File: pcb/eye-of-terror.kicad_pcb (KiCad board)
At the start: 4 copper layers, 200 x 200 mm, 225 parts, among them J1 Conn_01x02_Socket, J2 G-Switch GT-USB-7055E, J3 Conn_01x04, J4 Conn_01x04, J5 Conn_01x03, J6 Conn_01x02_Socket, J7 Conn_01x02_Socket, J8 Conn_01x03, Q1 IPT020N10N3, Q10 ALS-PT19-315C/L177/TR8, Q11 ALS-PT19-315C/L177/TR8, Q12 ALS-PT19-315C/L177/TR8, Q13 ALS-PT19-315C/L177/TR8, Q14 ALS-PT19-315C/L177/TR8, Q15 ALS-PT19-315C/L177/TR8, Q16 ALS-PT19-315C/L177/TR8, Q17 ALS-PT19-315C/L177/TR8, Q2 IPT020N10N3, Q3 IPT020N10N3, Q4 IPT020N10N3, Q5 IPT020N10N3, Q6 IPT020N10N3, Q7 ALS-PT19-315C/L177/TR8, Q8 ALS-PT19-315C/L177/TR8, Q9 ALS-PT19-315C/L177/TR8, SW1 SW_Push, SW2 SW_Push, U1 RP2350B, U2 TD1660, U3 AP63205WU-7, U4 LSM6DS3, U5 W25Q32JVSS, U7 DRV8353HRTAR, Y1 ABM8-272-T3

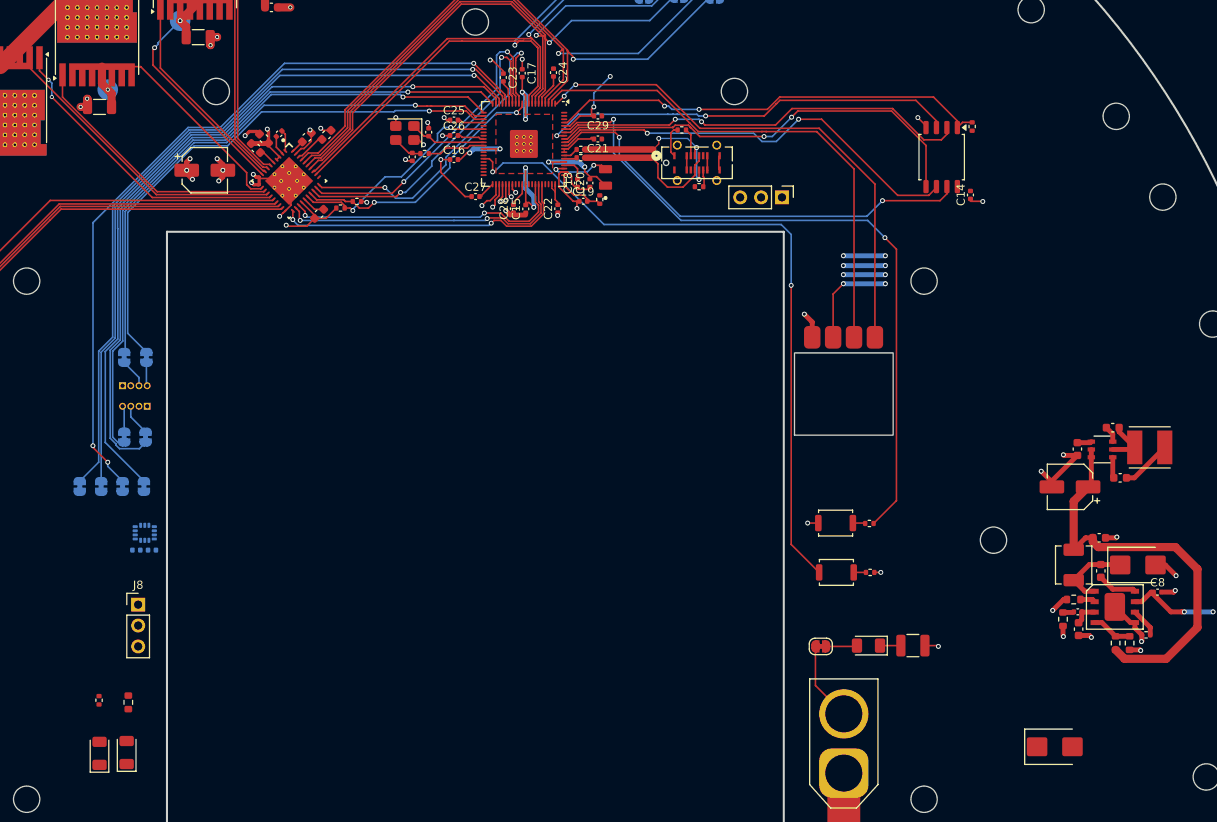
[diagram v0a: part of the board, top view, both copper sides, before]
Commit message: routed GPIO and debug LEDs
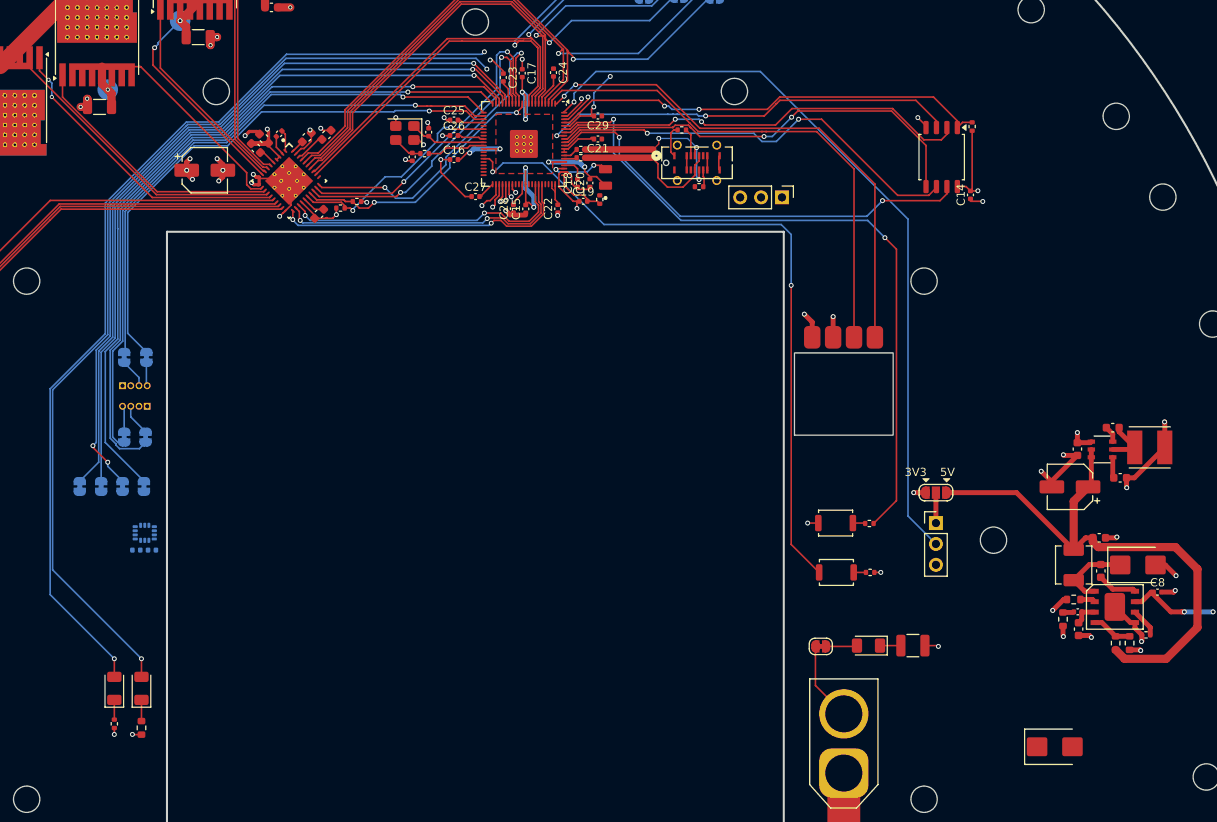
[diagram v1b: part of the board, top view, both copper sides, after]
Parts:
- added JP8: SolderJumper_3_Open, Jumper:SolderJumper-3_P1.3mm_Open_RoundedPad1.0x1.5mm_NumberLabels, F.Cu at (364.7, 193.3)
- moved J8 97.5 mm to (364.7, 197.0)
- moved D13 8.10 mm to (264.8, 217.1)
- moved D16 8.00 mm to (268.1, 217.1)
- moved R38 3.49 mm to (268.1, 221.9), turned to -90 degrees
- moved R35 3.41 mm to (264.8, 221.4), turned to -90 degrees
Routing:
- net /GREEN_LED_1: track 0.00 -> 138.1 mm, vias 0 -> 3
- net /BLUE_LED_1: track 0.00 -> 134.9 mm, vias 0 -> 3
- net /GPIO3: track 0.00 -> 92.9 mm, vias 0 -> 1
- net +5V: track 49.7 -> 68.0 mm
- net +3V3: track 82.8 -> 71.7 mm, vias 12 -> 10
- net Net-(J8-Pin_1): track 0.00 -> 3.70 mm
- net Net-(D16-K): track 0.00 -> 2.57 mm
- net Net-(D13-K): track 0.00 -> 2.40 mm
- net DGND: track 50.4 -> 52.2 mm, vias 20 -> 22
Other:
- board text added: "3V3"
- board text added: "5V"

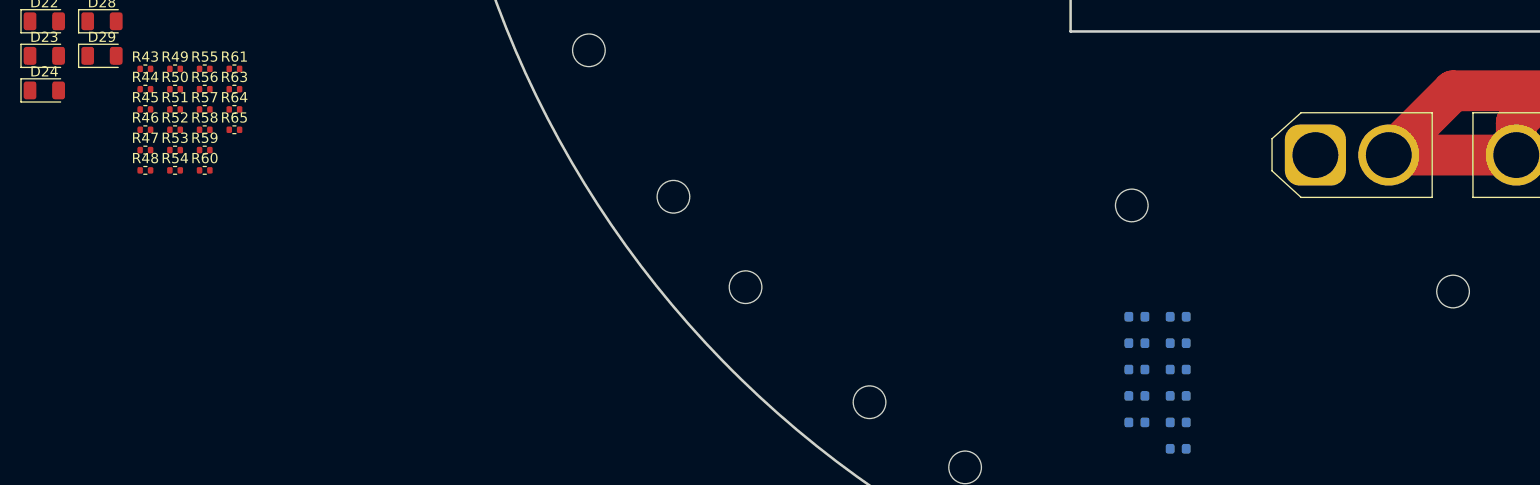
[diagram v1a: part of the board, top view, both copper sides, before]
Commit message: added placement dxf for encoders to layout
i think it lines up alright like this
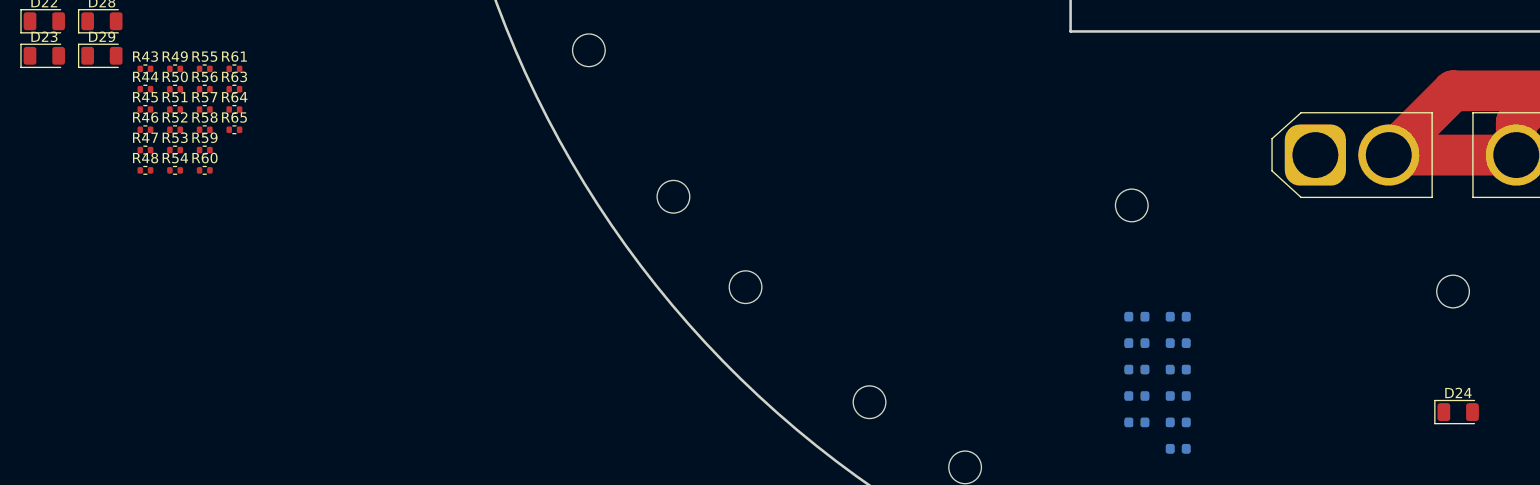
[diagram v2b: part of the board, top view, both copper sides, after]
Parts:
- moved D24 142.2 mm to (309.2, 273.9)

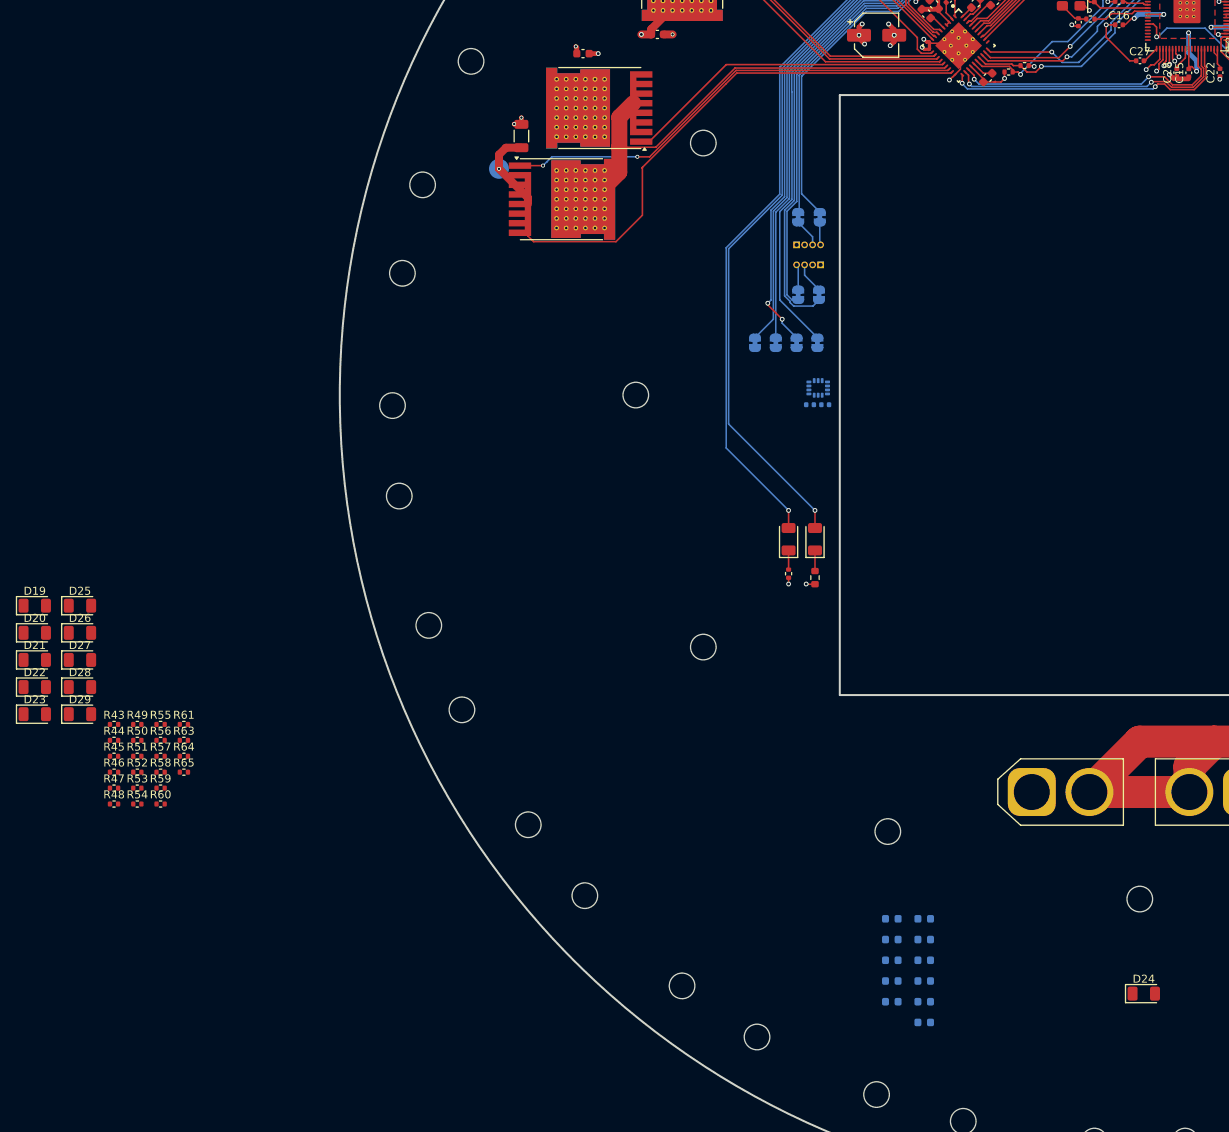
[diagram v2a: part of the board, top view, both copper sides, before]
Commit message: deleted 11th encoder pin (we only use 10)
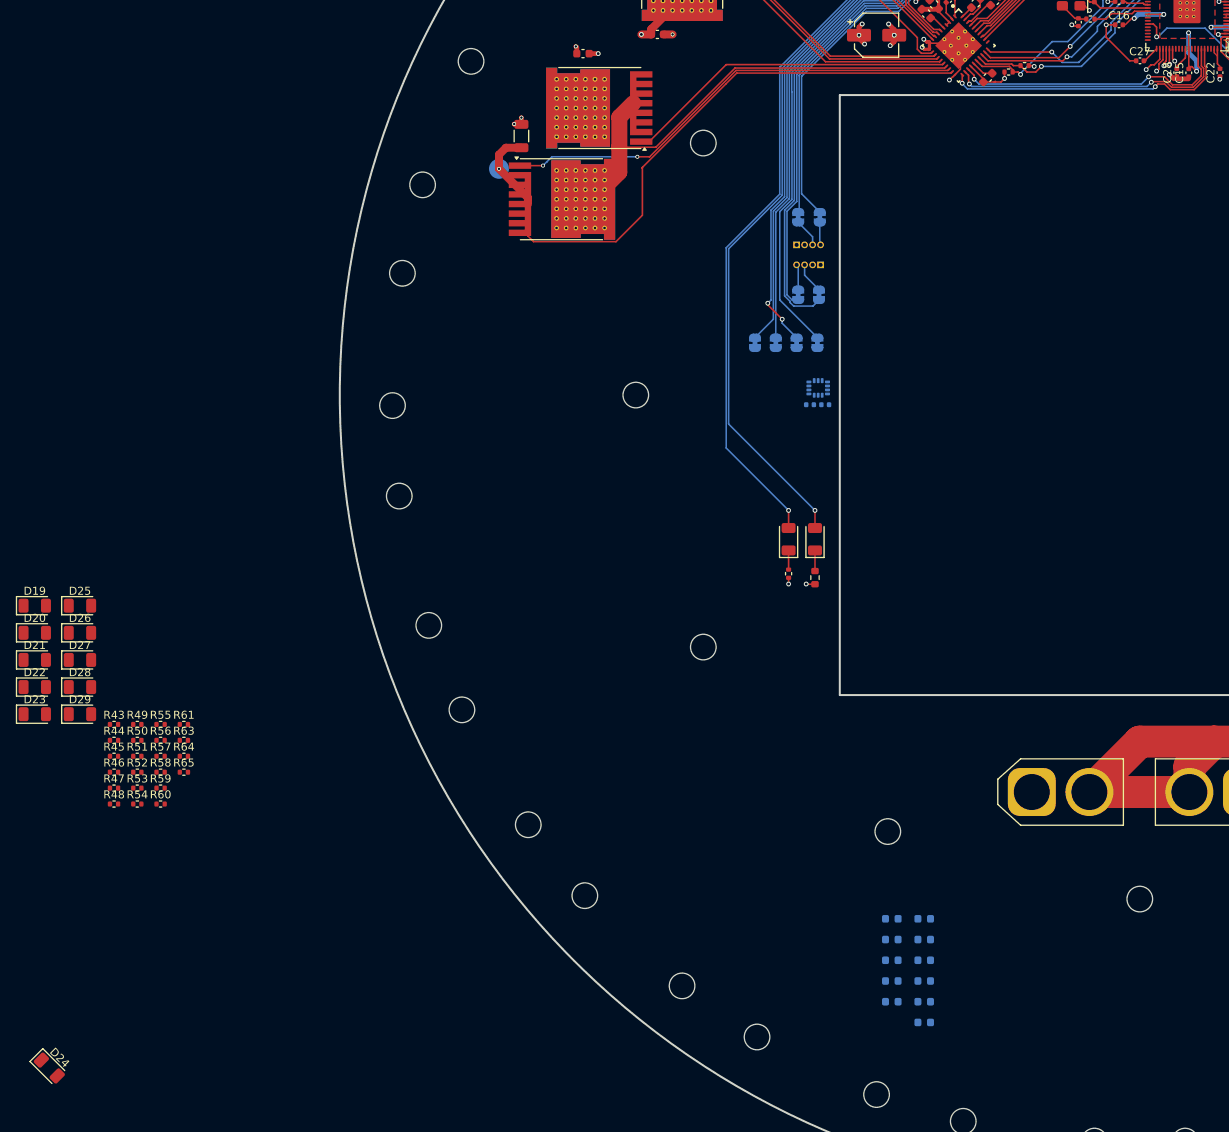
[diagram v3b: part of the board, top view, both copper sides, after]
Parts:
- moved D24 137.1 mm to (172.4, 283.2), turned to -45 degrees
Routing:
- net /ENC_SENSE_11: track 1.17 -> 0.00 mm, vias 1 -> 0
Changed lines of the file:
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@@
 	(footprint "Diode_SMD:D_1206_3216Metric"
 		(layer "F.Cu")
-		(at 309.2 273.9)
+		(at 172.39 283.2 -45)
 		(descr "Diode SMD 1206 (3216 Metric), square (rectangular) end terminal, IPC-7351 nominal, (Body size source: http://www.tortai-tech.com/upload/download/2011102023233369053.pdf), generated with kicad-footprint-generator")
 		(tags "diode")
 		(property "Reference" "D24"
-			(at 0 -1.83 0)
+			(at 0 -1.829999 135)
 			(layer "F.SilkS")
 			(effects
@@
 		)
 		(property "Value" "RED"
-			(at 0 1.83 0)
+			(at 0 1.829999 135)
 			(layer "F.Fab")
 			(effects
@@
 		)
 		(property "Datasheet" "~"
-			(at 0 0 0)
+			(at 0 0 135)
 			(layer "F.Fab")
 			(hide yes)
@@
 		)
 		(property "Description" "Light emitting diode"
-			(at 0 0 0)
+			(at 0 0 135)
 			(layer "F.Fab")
 			(hide yes)
@@
 		)
 		(property "Sim.Pins" "1=K 2=A"
-			(at 0 0 0)
+			(at 0 0 315)
 			(unlocked yes)
 			(layer "F.Fab")
@@
 		(duplicate_pad_numbers_are_jumpers no)
 		(fp_line
-			(start -2.285 -1.135)
-			(end -2.285 1.135)
+			(start -2.285 1.135)
+			(end 1.6 1.135)
 			(stroke
 				(width 0.12)
@@
 		)
 		(fp_line
-			(start -2.285 1.135)
-			(end 1.6 1.135)
+			(start -2.285 -1.135)
+			(end -2.285 1.135)
 			(stroke
 				(width 0.12)
@@
 		)
 		(fp_line
-			(start -2.28 -1.13)
-			(end 2.28 -1.13)
+			(start -2.28 1.13)
+			(end -2.28 -1.13)
 			(stroke
 				(width 0.05)
@@
 		)
 		(fp_line
-			(start -2.28 1.13)
-			(end -2.28 -1.13)
+			(start -2.28 -1.13)
+			(end 2.28 -1.13)
 			(stroke
 				(width 0.05)
@@
 		)
 		(fp_line
-			(start 2.28 -1.13)
-			(end 2.28 1.13)
+			(start 2.28 1.13)
+			(end -2.28 1.13)
 			(stroke
 				(width 0.05)
@@
 		)
 		(fp_line
-			(start 2.28 1.13)
-			(end -2.28 1.13)
+			(start 2.28 -1.13)
+			(end 2.28 1.13)
 			(stroke
 				(width 0.05)
@@
 		)
 		(fp_line
-			(start -1.6 -0.4)
-			(end -1.6 0.8)
+			(start -1.6 0.8)
+			(end 1.6 0.8)
 			(stroke
 				(width 0.1)
@@
 		)
 		(fp_line
-			(start -1.6 0.8)
-			(end 1.6 0.8)
+			(start -1.6 -0.4)
+			(end -1.6 0.8)
 			(stroke
 				(width 0.1)
@@
 		)
 		(fp_line
-			(start -1.2 -0.8)
+			(start -1.200001 -0.8)
 			(end -1.6 -0.4)
 			(stroke
@@
 		)
 		(fp_line
-			(start 1.6 -0.8)
-			(end -1.2 -0.8)
+			(start 1.6 0.8)
+			(end 1.6 -0.8)
 			(stroke
 				(width 0.1)
@@
 		)
 		(fp_line
-			(start 1.6 0.8)
-			(end 1.6 -0.8)
+			(start 1.6 -0.8)
+			(end -1.200001 -0.8)
 			(stroke
 				(width 0.1)
@@
 		)
 		(fp_text user "${REFERENCE}"
-			(at 0 0 0)
+			(at 0 0 135)
 			(layer "F.Fab")
 			(effects
@@
 		)
 		(pad "1" smd roundrect
-			(at -1.4 0)
+			(at -1.399999 0 315)
 			(size 1.25 1.75)
 			(layers "F.Cu" "F.Mask" "F.Paste")
@@
 		)
 		(pad "2" smd roundrect
-			(at 1.4 0)
+			(at 1.399999 0 315)
 			(size 1.25 1.75)
 			(layers "F.Cu" "F.Mask" "F.Paste")
@@
 			(type default)
 		)
+		(locked yes)
 		(layer "Dwgs.User")
 	)
@@
 			(type default)
 		)
+		(locked yes)
 		(layer "Dwgs.User")
 	)
@@
 			(type default)
 		)
+		(locked yes)
 		(layer "Dwgs.User")
 	)
@@
 			(type default)
 		)
+		(locked yes)
 		(layer "Dwgs.User")
 	)
@@
 			(type default)
 		)
+		(locked yes)
 		(layer "Dwgs.User")
 	)
@@
 			(type default)
 		)
+		(locked yes)
 		(layer "Dwgs.User")
 	)
@@
 			(type default)
 		)
+		(locked yes)
 		(layer "Dwgs.User")
 	)
@@
 			(type default)
 		)
+		(locked yes)
 		(layer "Dwgs.User")
 	)
@@
 			(type default)
 		)
+		(locked yes)
 		(layer "Dwgs.User")
 	)
@@
 			(type default)
 		)
+		(locked yes)
 		(layer "Dwgs.User")
 	)
@@
 			(type default)
 		)
+		(locked yes)
 		(layer "Dwgs.User")
 	)
@@
 			(type default)
 		)
+		(locked yes)
 		(layer "Dwgs.User")
 	)
@@
 			(type default)
 		)
+		(locked yes)
 		(layer "Dwgs.User")
 	)
@@
 			(type default)
 		)
+		(locked yes)
 		(layer "Dwgs.User")
 	)
@@
 			(type default)
 		)
+		(locked yes)
 		(layer "Dwgs.User")
 	)
@@
 			(type default)
 		)
+		(locked yes)
 		(layer "Dwgs.User")
 	)
@@
 			(type default)
 		)
+		(locked yes)
 		(layer "Dwgs.User")
 	)
@@
 			(type default)
 		)
+		(locked yes)
 		(layer "Dwgs.User")
 	)
@@
 			(type default)
 		)
+		(locked yes)
 		(layer "Dwgs.User")
 	)
@@
 			(type default)
 		)
+		(locked yes)
 		(layer "Dwgs.User")
 	)
@@
 			(type default)
 		)
+		(locked yes)
 		(layer "Dwgs.User")
 	)
@@
 			(type default)
 		)
+		(locked yes)
 		(layer "Dwgs.User")
 	)
@@
 			(type default)
 		)
+		(locked yes)
 		(layer "Dwgs.User")
 	)
@@
 			(type default)
 		)
+		(locked yes)
 		(layer "Dwgs.User")
 	)
@@
 			(type default)
 		)
+		(locked yes)
 		(layer "Dwgs.User")
 	)
@@
 			(type default)
 		)
+		(locked yes)
 		(layer "Dwgs.User")
 	)
@@
 			(type default)
 		)
+		(locked yes)
 		(layer "Dwgs.User")
 	)
@@
 			(type default)
 		)
+		(locked yes)
 		(layer "Dwgs.User")
 	)
@@
 			(type default)
 		)
+		(locked yes)
 		(layer "Dwgs.User")
 	)
@@
 			(type default)
 		)
+		(locked yes)
 		(layer "Dwgs.User")
 	)
@@
 			(type default)
 		)
+		(locked yes)
 		(layer "Dwgs.User")
 	)
@@
 			(type default)
 		)
+		(locked yes)
 		(layer "Dwgs.User")
 	)
@@
 			(type default)
 		)
+		(locked yes)
 		(layer "Dwgs.User")
 	)
@@
 			(type default)
 		)
+		(locked yes)
 		(layer "Dwgs.User")
 	)
@@
 			(type default)
 		)
+		(locked yes)
 		(layer "Dwgs.User")
 	)
@@
 			(type default)
 		)
+		(locked yes)
 		(layer "Dwgs.User")
 	)
@@
 			(type default)
 		)
+		(locked yes)
 		(layer "Dwgs.User")
 	)
@@
 			(type default)
 		)
+		(locked yes)
 		(layer "Dwgs.User")
 	)
@@
 			(type default)
 		)
+		(locked yes)
 		(layer "Dwgs.User")
 	)
@@
 			(type default)
 		)
+		(locked yes)
 		(layer "Dwgs.User")
 	)
@@
 			(type default)
 		)
+		(locked yes)
 		(layer "Dwgs.User")
 	)
@@
 			(type default)
 		)
+		(locked yes)
 		(layer "Dwgs.User")
 	)
@@
 			(type default)
 		)
+		(locked yes)
 		(layer "Dwgs.User")
 	)
@@
 			(type default)
 		)
+		(locked yes)
 		(layer "Dwgs.User")
 	)
@@
 	)
 	(segment
-		(start 313.2 155.797)
-		(end 313.2 156.4)
-		(width 0.2)
-		(layer "F.Cu")
-		(net "/ENC_SENSE_11")
-	)
-	(segment
-		(start 313.2 156.4)
-		(end 313.6 156.8)
-		(width 0.2)
-		(layer "F.Cu")
-		(net "/ENC_SENSE_11")
-	)
-	(via
-		(at 313.6 156.8)
-		(size 0.6)
-		(drill 0.35)
-		(layers "F.Cu" "B.Cu")
-		(capping no)
-		(covering
-			(front no)
-			(back no)
-		)
-		(plugging
-			(front no)
-			(back no)
-		)
-		(filling no)
-		(net "/ENC_SENSE_11")
-	)
-	(segment
 		(start 336.97 154.135)
 		(end 336.9 154.065)
@@
 	)
 	(group ""
+		(locked yes)
 		(members "0744a833-d7ef-42d8-9eca-3342a2bef08c" "08aa76d5-c39c-4b37-bc9b-3138c20e0c3d"
 			"0fad0084-5e44-4c27-b067-b843977a380a" "100a4a0c-d60a-44d2-836b-6ce4470c00dd"
